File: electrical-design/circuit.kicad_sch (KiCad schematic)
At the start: 53 parts, among them J1 AVR-ISP-10, Q1 2N3906, Q2 2N3906, Q3 2N3906, Q4 2N3906, SW1 Reset Button, SW2 DS02C-254-1L-04BE, SW3 Reset Button, U1 ATmega8A-P, U2 LTC-4627JR, U3 NE555P, Y1 16MHz

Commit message: Started Design For Rev 1.1
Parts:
- added C2: 0.1uF, Capacitor_THT:C_Disc_D3.0mm_W2.0mm_P2.50mm, symbol Device:C_Small
- added R1: 330, Resistor_THT:R_Axial_DIN0204_L3.6mm_D1.6mm_P5.08mm_Horizontal, symbol Device:R_Small
- SW1: footprint Button_Switch_THT:SW_PUSH_6mm_H5mm -> Button_Switch_THT:SW_PUSH_6mm
- renumbered C7 to C1, C1 to C3, C2 to C4, C3 to C5, C4 to C7, C5 to C8, H4 to H1, H1 to H2, H2 to H4, R25 to R10, R3 to R11, R15 to R12, R14 to R13, R13 to R14, R12 to R15, R7 to R18, R8 to R19, R1 to R2, R11 to R20, R19 to R21, R18 to R22, R20 to R23, R21 to R24, R22 to R25, R23 to R26, R5 to R3, R10 to R4, R4 to R5, R9 to R7, R2 to R8, R24 to R9, TP2 to TP1, TP1 to TP2
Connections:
- net GND: now also C2.1
- net ~{RESET}: now also C2.2, R1.1; no longer SW1.2
- new net: R1.2, SW1.2
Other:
- moved on the sheet: C1, C3, C4, C5, C6, D1, D2, R10, R11, R2, R3, R4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

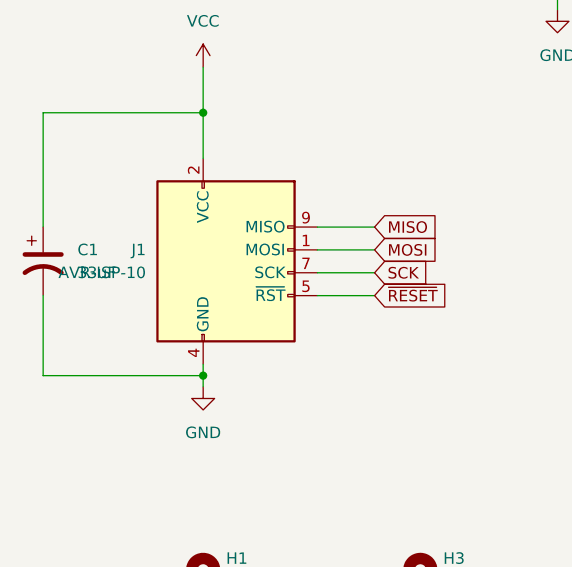
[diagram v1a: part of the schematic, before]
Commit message: Changed ISP-10 Footprint to ISP-6
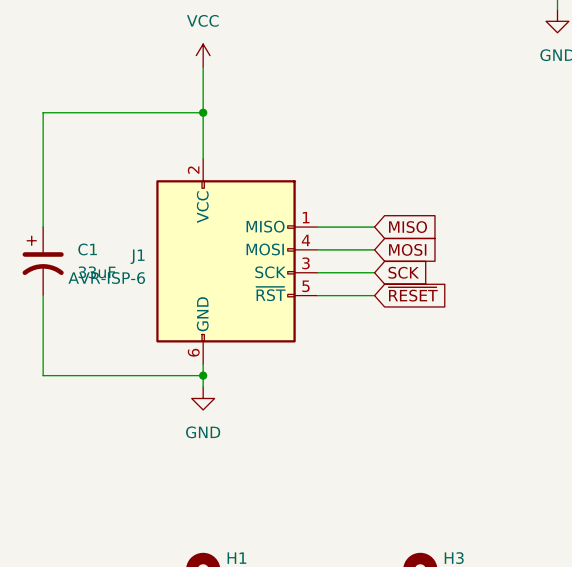
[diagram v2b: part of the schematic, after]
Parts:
- removed J1: AVR-ISP-10, Connector_IDC:IDC-Header_2x05_P2.54mm_Vertical, symbol Connector:AVR-ISP-10
- added J1: AVR-ISP-6, Connector_IDC:IDC-Header_2x03_P2.54mm_Vertical, symbol Connector:AVR-ISP-6
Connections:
- net GND: now also J1.6 (GND)
- net MISO: now also J1.1 (MISO)
- net MOSI: now also J1.4 (MOSI)
- net SCK: now also J1.3 (SCK)
- net VCC: now also J1.2 (VCC)
- net ~{RESET}: now also J1.5 (~{RST})

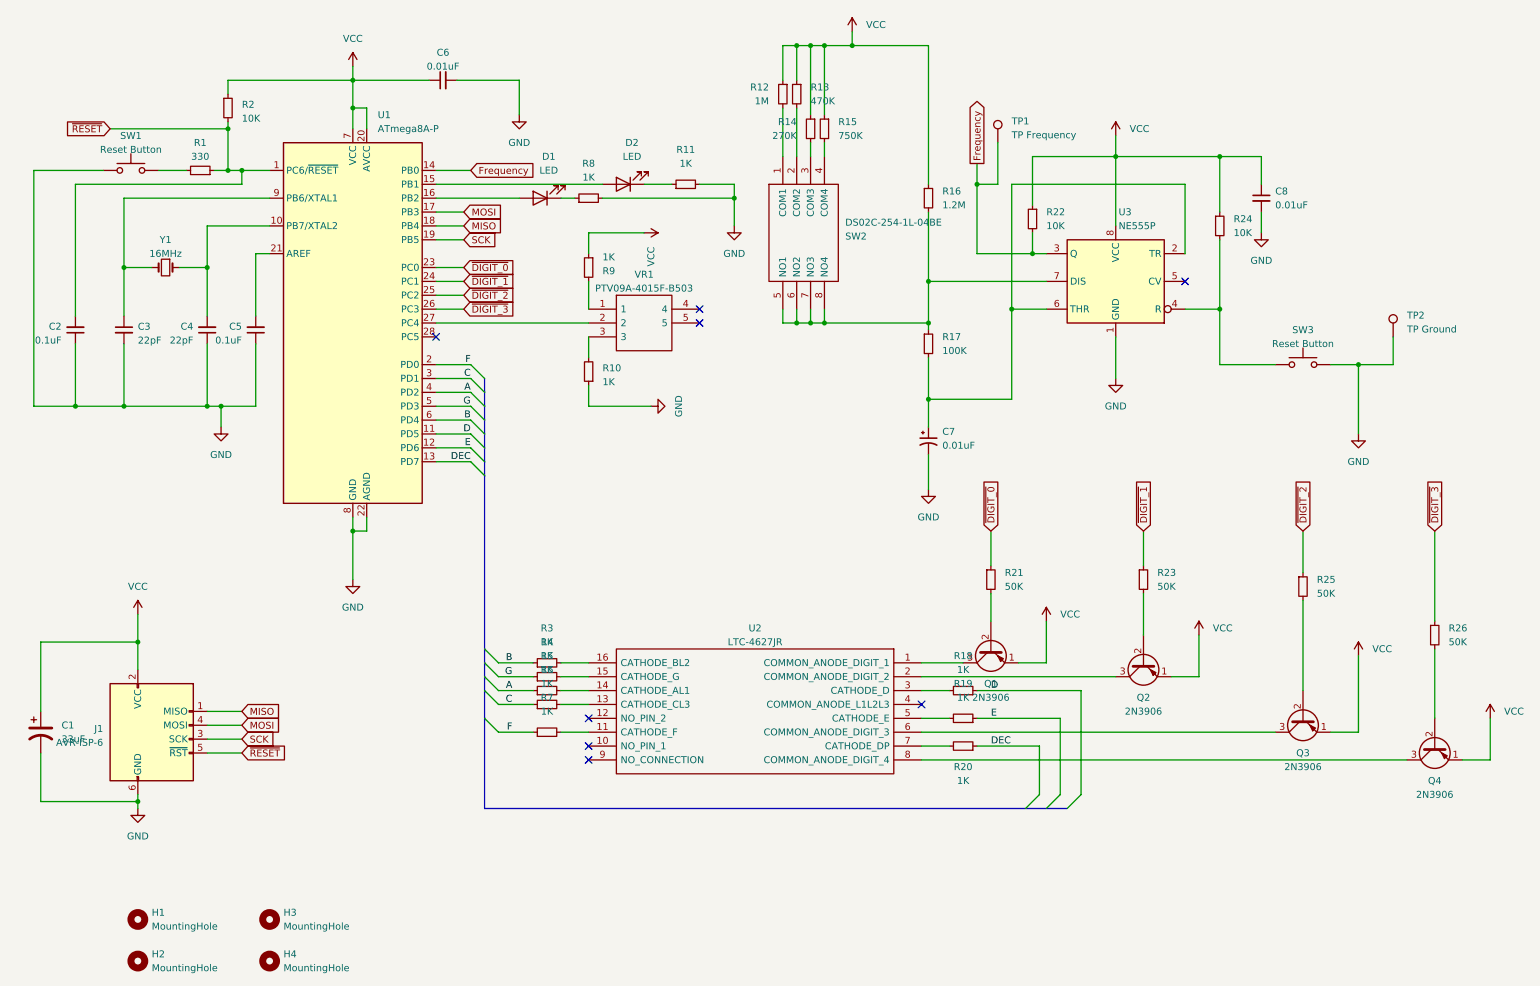
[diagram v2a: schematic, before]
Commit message: Updated THT Resistor Footprint
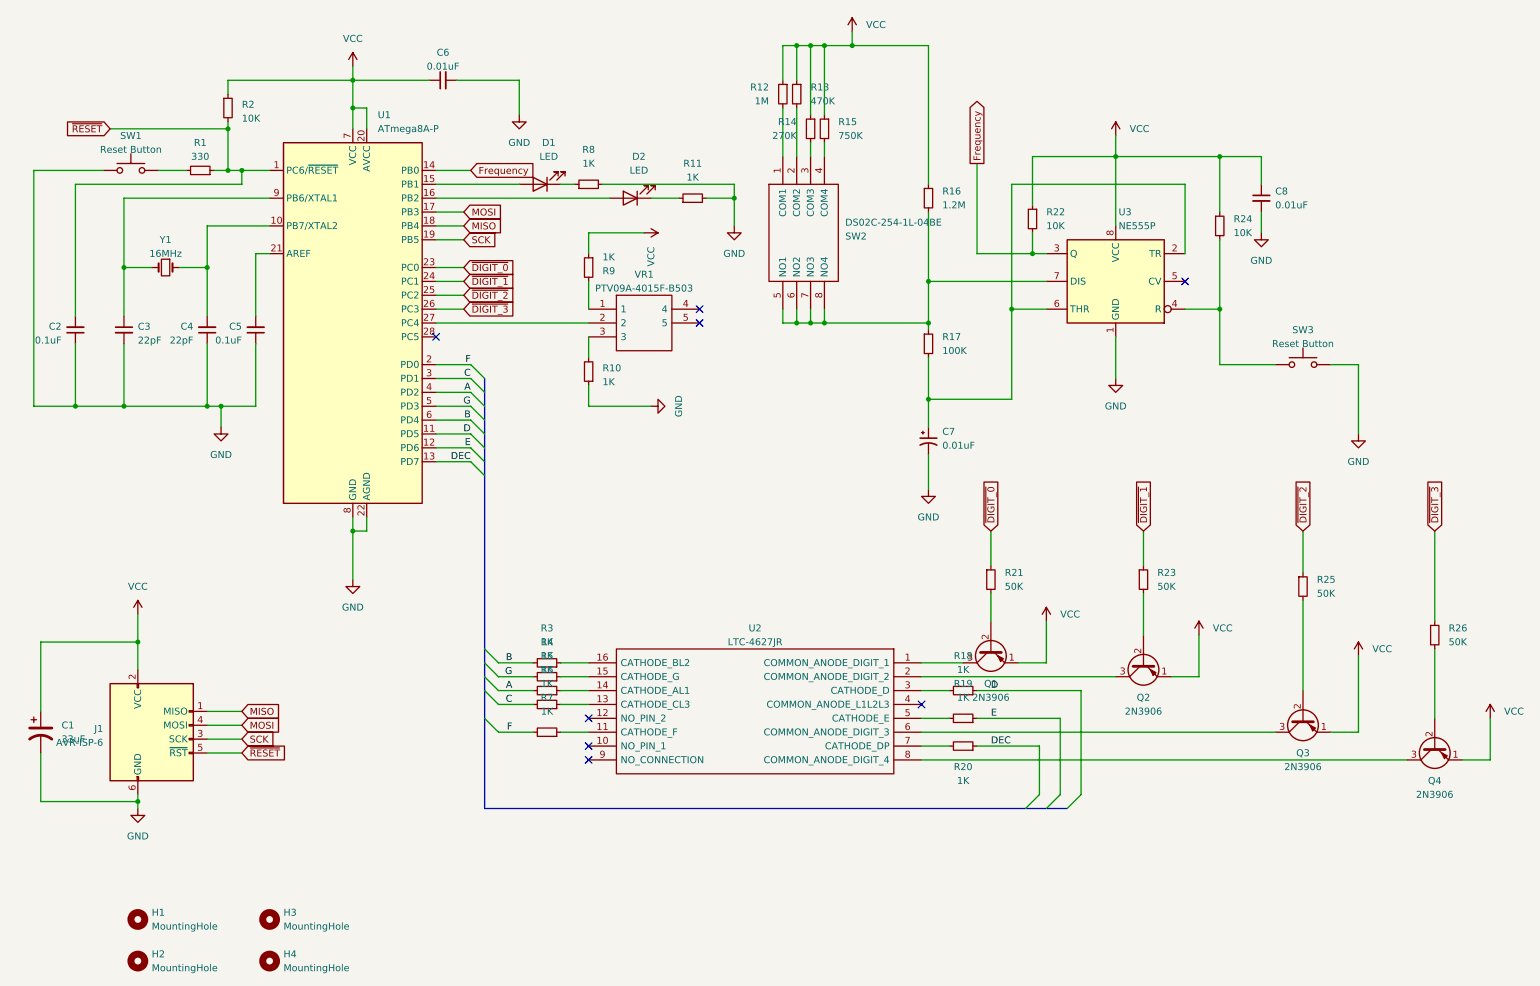
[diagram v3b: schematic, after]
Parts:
- removed TP1: TP Frequency, TestPoint:TestPoint_THTPad_2.0x2.0mm_Drill1.0mm, symbol Connector:TestPoint
- removed TP2: TP Ground, TestPoint:TestPoint_THTPad_2.0x2.0mm_Drill1.0mm, symbol Connector:TestPoint
- R1, R10, R11, R12, R13, R14, R15, R16, R17, R18, R19, R2, R20, R21, R22, R23, R24, R25, R26, R3, R4, R5, R6, R7, R8, R9: footprint Resistor_THT:R_Axial_DIN0204_L3.6mm_D1.6mm_P5.08mm_Horizontal -> Resistor_THT:R_Axial_DIN0207_L6.3mm_D2.5mm_P7.62mm_Horizontal
- SW2: footprint DS02C2541L04BE -> DIP Switch:DS02C2541L04BE
- VR1: footprint PTV09A4020FB103 -> Potentiometer:PTV09A4020FB103
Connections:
- net A: now also R5.2; no longer R5.1
- net B: now also R3.2; no longer R3.1
- net C: now also R6.2; no longer R6.1
- net F: now also R7.2; no longer R7.1
- net G: now also R4.2; no longer R4.1
- net at U2.11 (CATHODE_F): now also R7.1; no longer R7.2
- net at U1.15 (PB1): now also D1.2 (A); no longer D2.2 (A)
- net at U1.16 (PB2): now also D2.2 (A); no longer D1.2 (A)
- net at U2.14 (CATHODE_AL1): now also R5.1; no longer R5.2
- net at U2.13 (CATHODE_CL3): now also R6.1; no longer R6.2
- net at U2.16 (CATHODE_BL2): now also R3.1; no longer R3.2
- net at U2.15 (CATHODE_G): now also R4.1; no longer R4.2
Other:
- moved on the sheet: D1, D2, R11, R3, R4, R5, R6, R7, R8

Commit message: Completed Version 1.1
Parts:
- removed C1: 33uF, Capacitor_THT:CP_Radial_D4.0mm_P2.00mm, symbol Device:C_Polarized_US
- J1: footprint Connector_IDC:IDC-Header_2x03_P2.54mm_Vertical -> Connector_PinHeader_2.54mm:PinHeader_2x03_P2.54mm_Vertical
- renumbered C2 to C1, C3 to C2, C4 to C3, C5 to C4, C6 to C5, C7 to C6, C8 to C7
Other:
- title: (none) -> ATMEGA8A Tutorial Board A
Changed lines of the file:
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@@
 (kicad_sch (version 20230121) (generator eeschema)
   (paper "A4")
+  (title_block
+    (title "ATMEGA8A Tutorial Board A")
+    (date "2023-03-11")
+    (rev "1.1")
+  )
   (junction (at 156.21 69.85) (diameter 0) (color 0 0 0 0)
   )
@@
   (junction (at 233.68 39.37) (diameter 0) (color 0 0 0 0)
   )
-  (junction (at 35.56 157.48) (diameter 0) (color 0 0 0 0)
-  )
   (junction (at 233.68 67.31) (diameter 0) (color 0 0 0 0)
   )
@@
   )
   (junction (at 158.75 69.85) (diameter 0) (color 0 0 0 0)
-  )
-  (junction (at 35.56 128.27) (diameter 0) (color 0 0 0 0)
   )
   (junction (at 24.13 85.09) (diameter 0) (color 0 0 0 0)
@@
     (stroke (width 0) (type default))
   )
-  (wire (pts (xy 17.78 140.97) (xy 17.78 128.27))
-    (stroke (width 0) (type default))
-  )
   (wire (pts (xy 33.02 59.69) (xy 33.02 68.58))
     (stroke (width 0) (type default))
@@
     (stroke (width 0) (type default))
   )
-  (wire (pts (xy 17.78 128.27) (xy 35.56 128.27))
-    (stroke (width 0) (type default))
-  )
   (wire (pts (xy 179.07 134.62) (xy 214.63 134.62))
     (stroke (width 0) (type default))
@@
     (stroke (width 0) (type default))
   )
-  (wire (pts (xy 35.56 128.27) (xy 35.56 133.35))
-    (stroke (width 0) (type default))
-  )
   (wire (pts (xy 90.17 54.61) (xy 95.25 54.61))
     (stroke (width 0) (type default))
@@
     (stroke (width 0) (type default))
   )
-  (wire (pts (xy 35.56 123.19) (xy 35.56 128.27))
+  (wire (pts (xy 35.56 123.19) (xy 35.56 133.35))
     (stroke (width 0) (type default))
   )
@@
     (stroke (width 0) (type default))
   )
-  (wire (pts (xy 17.78 157.48) (xy 35.56 157.48))
-    (stroke (width 0) (type default))
-  )
-  (wire (pts (xy 35.56 157.48) (xy 35.56 158.75))
+  (wire (pts (xy 35.56 156.21) (xy 35.56 158.75))
     (stroke (width 0) (type default))
   )
@@
     (stroke (width 0) (type default))
   )
-  (wire (pts (xy 17.78 148.59) (xy 17.78 157.48))
-    (stroke (width 0) (type default))
-  )
   (wire (pts (xy 180.34 69.85) (xy 180.34 71.12))
     (stroke (width 0) (type default))
@@
   )
   (wire (pts (xy 195.58 83.82) (xy 180.34 83.82))
-    (stroke (width 0) (type default))
-  )
-  (wire (pts (xy 35.56 156.21) (xy 35.56 157.48))
     (stroke (width 0) (type default))
   )
@@
   (symbol (lib_id "Device:C_Small") (at 241.3 46.99 0) (unit 1)
     (in_bom yes) (on_board yes) (dnp no) (fields_autoplaced)
-    (property "Reference" "C8" (at 243.84 45.7262 0)
+    (property "Reference" "C7" (at 243.84 45.7262 0)
       (effects (font (size 1.27 1.27)) (justify left))
     )
@@
       (project "circuit"
         (path "/e92f8e40-1e47-4cd0-a865-c589067a003b"
-          (reference "C8") (unit 1)
+          (reference "C7") (unit 1)
         )
       )
@@
     )
   )
-  (symbol (lib_id "Device:C_Polarized_US") (at 17.78 144.78 0) (unit 1)
-    (in_bom yes) (on_board yes) (dnp no)
-    (property "Reference" "C1" (at 21.59 143.51 0)
-      (effects (font (size 1.27 1.27)) (justify left))
-    )
-    (property "Value" "33uF" (at 21.59 146.05 0)
-      (effects (font (size 1.27 1.27)) (justify left))
-    )
-    (property "Footprint" "Capacitor_THT:CP_Radial_D4.0mm_P2.00mm" (at 17.78 144.78 0)
-      (effects (font (size 1.27 1.27)) hide)
-    )
-    (property "Datasheet" "~" (at 17.78 144.78 0)
-      (effects (font (size 1.27 1.27)) hide)
-    )
-    (pin "1")
-    (pin "2")
-    (instances
-      (project "circuit"
-        (path "/e92f8e40-1e47-4cd0-a865-c589067a003b"
-          (reference "C1") (unit 1)
-        )
-      )
-    )
-  )
   (symbol (lib_id "Device:R_Small") (at 156.21 27.94 0) (mirror y) (unit 1)
     (in_bom yes) (on_board yes) (dnp no) (fields_autoplaced)
@@
   (symbol (lib_id "Device:C_Small") (at 33.02 71.12 0) (unit 1)
     (in_bom yes) (on_board yes) (dnp no) (fields_autoplaced)
-    (property "Reference" "C3" (at 35.56 70.4913 0)
+    (property "Reference" "C2" (at 35.56 70.4913 0)
       (effects (font (size 1.27 1.27)) (justify left))
     )
@@
       (project "circuit"
         (path "/e92f8e40-1e47-4cd0-a865-c589067a003b"
-          (reference "C3") (unit 1)
+          (reference "C2") (unit 1)
         )
       )
@@
   (symbol (lib_id "Device:C_Small") (at 24.13 71.12 0) (mirror x) (unit 1)
     (in_bom yes) (on_board yes) (dnp no) (fields_autoplaced)
-    (property "Reference" "C2" (at 21.59 70.4786 0)
+    (property "Reference" "C1" (at 21.59 70.4786 0)
       (effects (font (size 1.27 1.27)) (justify right))
     )
@@
       (project "circuit"
         (path "/e92f8e40-1e47-4cd0-a865-c589067a003b"
-          (reference "C2") (unit 1)
+          (reference "C1") (unit 1)
         )
       )
@@
   (symbol (lib_id "Device:C_Small") (at 48.26 71.12 0) (mirror x) (unit 1)
     (in_bom yes) (on_board yes) (dnp no) (fields_autoplaced)
-    (property "Reference" "C4" (at 45.72 70.4786 0)
+    (property "Reference" "C3" (at 45.72 70.4786 0)
       (effects (font (size 1.27 1.27)) (justify right))
     )
@@
       (project "circuit"
         (path "/e92f8e40-1e47-4cd0-a865-c589067a003b"
-          (reference "C4") (unit 1)
+          (reference "C3") (unit 1)
         )
       )
@@
   (symbol (lib_id "Device:C_Small") (at 91.44 25.4 90) (unit 1)
     (in_bom yes) (on_board yes) (dnp no) (fields_autoplaced)
-    (property "Reference" "C6" (at 91.4463 20.32 90)
+    (property "Reference" "C5" (at 91.4463 20.32 90)
       (effects (font (size 1.27 1.27)))
     )
@@
       (project "circuit"
         (path "/e92f8e40-1e47-4cd0-a865-c589067a003b"
-          (reference "C6") (unit 1)
+          (reference "C5") (unit 1)
         )
       )
@@
   (symbol (lib_id "Device:C_Small") (at 57.15 71.12 0) (mirror x) (unit 1)
     (in_bom yes) (on_board yes) (dnp no) (fields_autoplaced)
-    (property "Reference" "C5" (at 54.61 70.4786 0)
+    (property "Reference" "C4" (at 54.61 70.4786 0)
       (effects (font (size 1.27 1.27)) (justify right))
     )
@@
       (project "circuit"
         (path "/e92f8e40-1e47-4cd0-a865-c589067a003b"
-          (reference "C5") (unit 1)
+          (reference "C4") (unit 1)
         )
       )
@@
   (symbol (lib_id "Device:C_Polarized_Small_US") (at 180.34 91.44 0) (unit 1)
     (in_bom yes) (on_board yes) (dnp no) (fields_autoplaced)
-    (property "Reference" "C7" (at 182.88 89.7381 0)
+    (property "Reference" "C6" (at 182.88 89.7381 0)
       (effects (font (size 1.27 1.27)) (justify left))
     )
@@
       (project "circuit"
         (path "/e92f8e40-1e47-4cd0-a865-c589067a003b"
-          (reference "C7") (unit 1)
+          (reference "C6") (unit 1)
         )
       )
@@
       (effects (font (size 1.27 1.27)) (justify right))
     )
-    (property "Footprint" "Connector_IDC:IDC-Header_2x03_P2.54mm_Vertical" (at 31.75 144.78 90)
-      (effects (font (size 1.27 1.27)) hide)
-    )
+    (property "Footprint" "Connector_PinHeader_2.54mm:PinHeader_2x03_P2.54mm_Vertical" (at 31.75 144.78 90)
+      (effects (font (size 1.27 1.27)) hide)
+    )
